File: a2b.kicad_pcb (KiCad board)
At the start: 2 copper layers, 58.4 x 67.9 mm, 16 parts, among them J1 M20-9990246

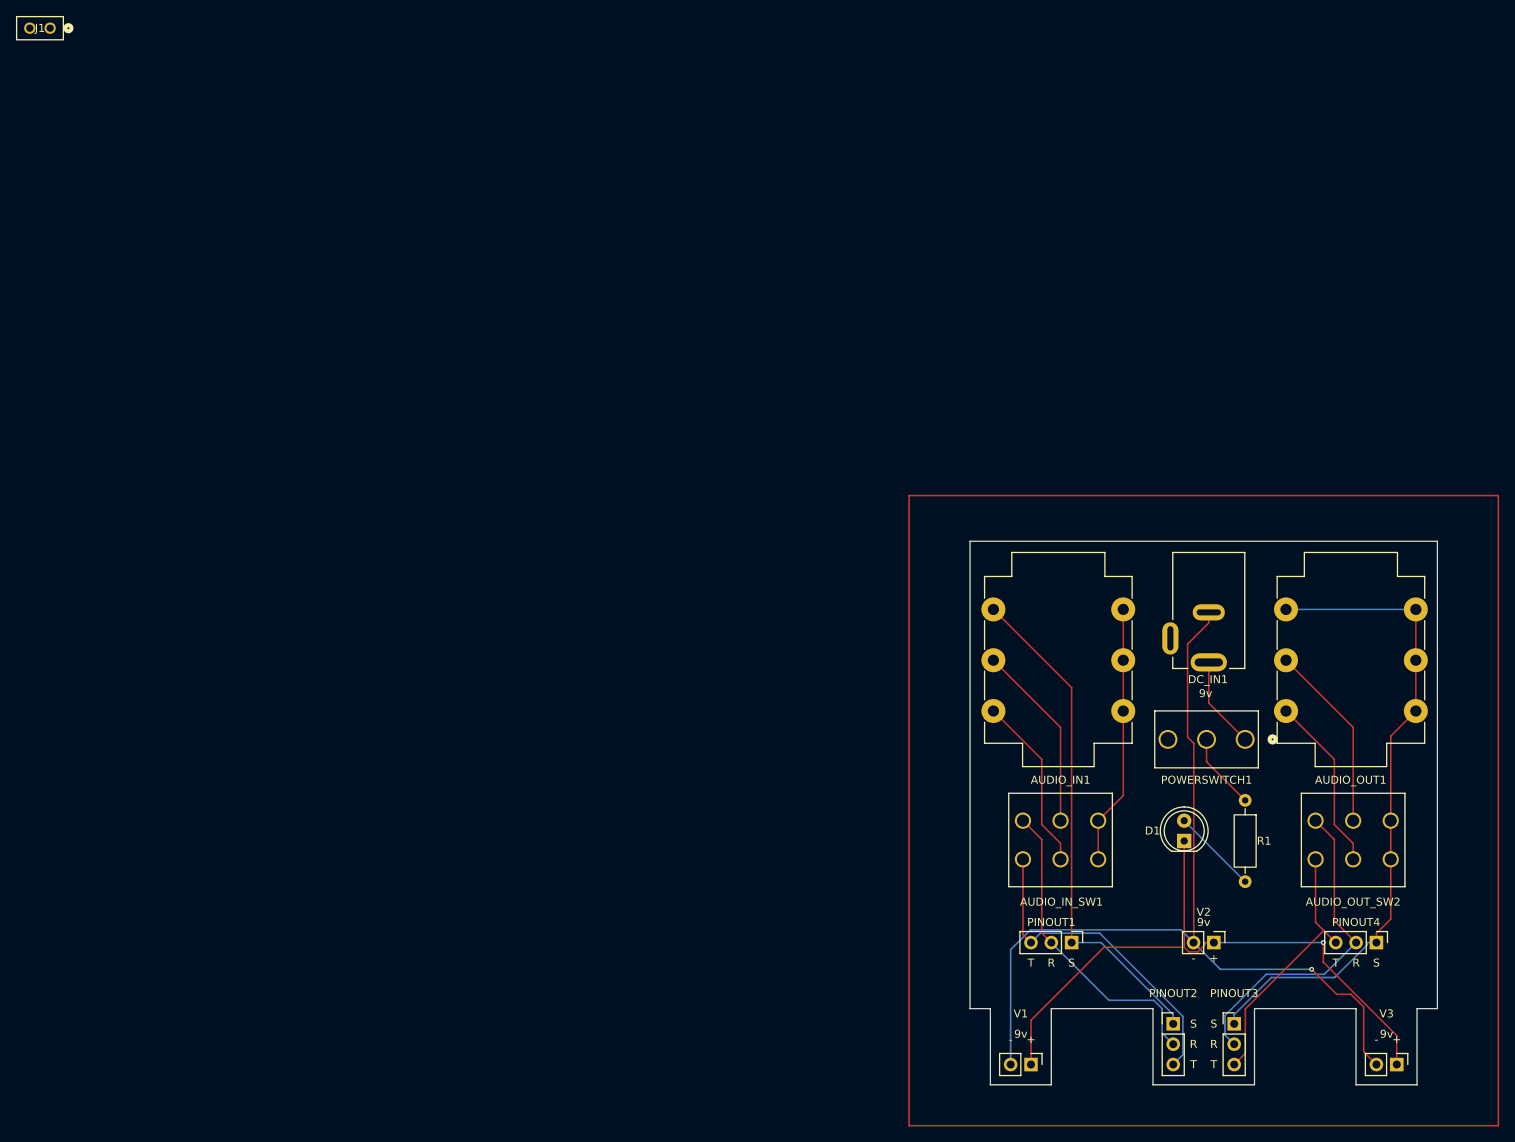
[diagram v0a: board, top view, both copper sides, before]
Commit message: swap to dip switches Signed-off-by: MrMentalFlower <samuelejpike@gmail.com>
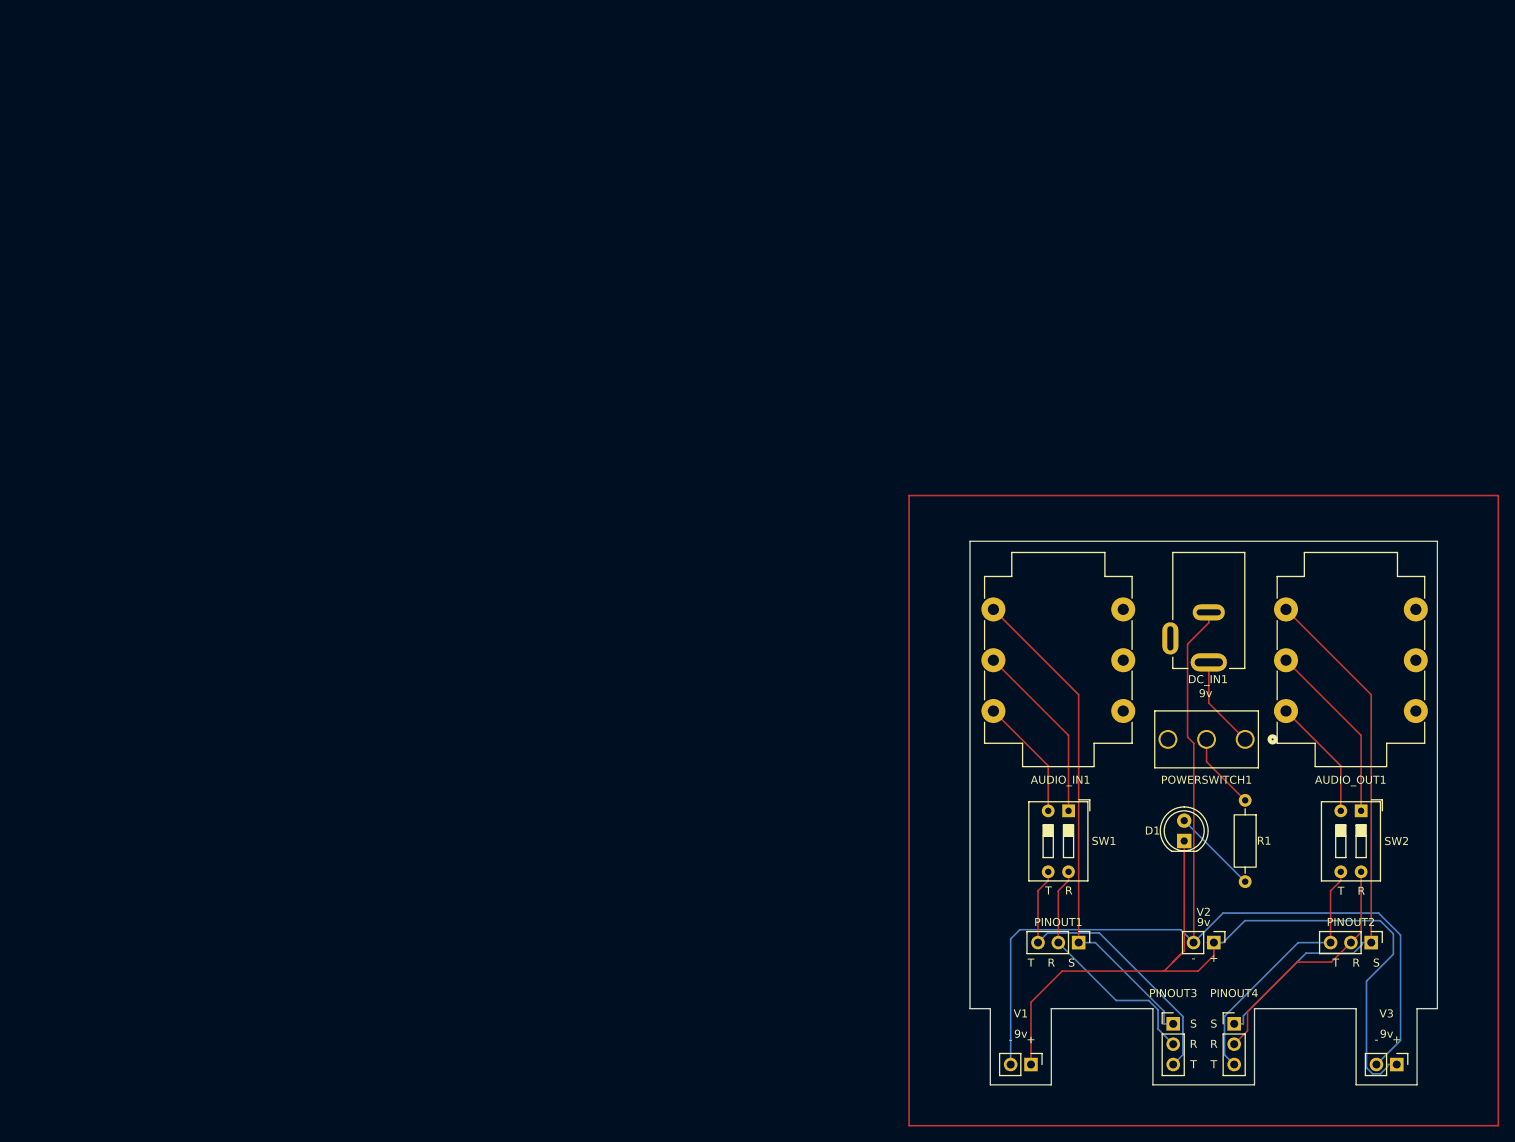
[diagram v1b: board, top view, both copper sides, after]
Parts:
- removed AUDIO_IN_SW1, AUDIO_OUT_SW2: ANT21SECQE, ANT21SECQE:SW6_ANT21SECQE_CRS
- removed J1: M20-9990246, M20-9990246:CONN2_M20-999_1x2_HRW
- added SW1: SW_DIP_x02, Button_Switch_THT:SW_DIP_SPSTx02_Slide_9.78x7.26mm_W7.62mm_P2.54mm, F.Cu at (131.7, 100.4)
- added SW2: SW_DIP_x02, Button_Switch_THT:SW_DIP_SPSTx02_Slide_9.78x7.26mm_W7.62mm_P2.54mm, F.Cu at (168.3, 100.4)
- moved PINOUT1 0.88 mm to (133.0, 116.8)
- moved PINOUT2 0.65 mm to (169.5, 116.8)
- renumbered PINOUT4 to PINOUT2, PINOUT2 to PINOUT3, PINOUT3 to PINOUT4
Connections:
- AUDIO_IN1 pad RN: Net-(AUDIO_IN1-PadRN) -> unconnected-(AUDIO_IN1-PadRN)
- AUDIO_IN1 pad SN: Net-(AUDIO_IN1-PadRN) -> unconnected-(AUDIO_IN1-PadSN)
- AUDIO_IN1 pad TN: Net-(AUDIO_IN1-PadRN) -> unconnected-(AUDIO_IN1-PadTN)
- AUDIO_OUT1 pad RN: Net-(AUDIO_OUT1-PadRN) -> unconnected-(AUDIO_OUT1-PadRN)
- AUDIO_OUT1 pad S: Net-(AUDIO_OUT1-PadRN) -> Net-(AUDIO_OUT1-PadS)
- AUDIO_OUT1 pad SN: Net-(AUDIO_OUT1-PadRN) -> unconnected-(AUDIO_OUT1-PadSN)
- AUDIO_OUT1 pad TN: Net-(AUDIO_OUT1-PadRN) -> unconnected-(AUDIO_OUT1-PadTN)
- PINOUT2 pad 1: Net-(AUDIO_OUT1-PadRN) -> Net-(AUDIO_OUT1-PadS)
- PINOUT4 pad 1: Net-(AUDIO_OUT1-PadRN) -> Net-(AUDIO_OUT1-PadS)
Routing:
- net Net-(AUDIO_OUT1-PadRN): track 82.7 -> 0.00 mm
- net Net-(AUDIO_OUT1-PadS): track 0.00 -> 68.1 mm
- net Net-(AUDIO_IN1-PadRN): track 32.5 -> 0.00 mm
- net Net-(D1-K): track 79.1 -> 103.9 mm, vias 1 -> 0
- net Net-(DC_IN1-PadSLEEVE): track 114.1 -> 128.4 mm, vias 1 -> 0
- net Net-(PINOUT2-Pad2): track 41.6 -> 30.6 mm
- net Net-(PINOUT1-Pad2): track 39.0 -> 30.4 mm
- net Net-(AUDIO_OUT1-PadT): track 22.0 -> 15.3 mm
- net Net-(AUDIO_IN1-PadT): track 22.0 -> 15.3 mm
- net Net-(PINOUT1-Pad3): track 41.1 -> 38.8 mm
- net Net-(AUDIO_OUT1-PadR): track 23.5 -> 22.7 mm
- net Net-(AUDIO_IN1-PadR): track 23.5 -> 22.7 mm

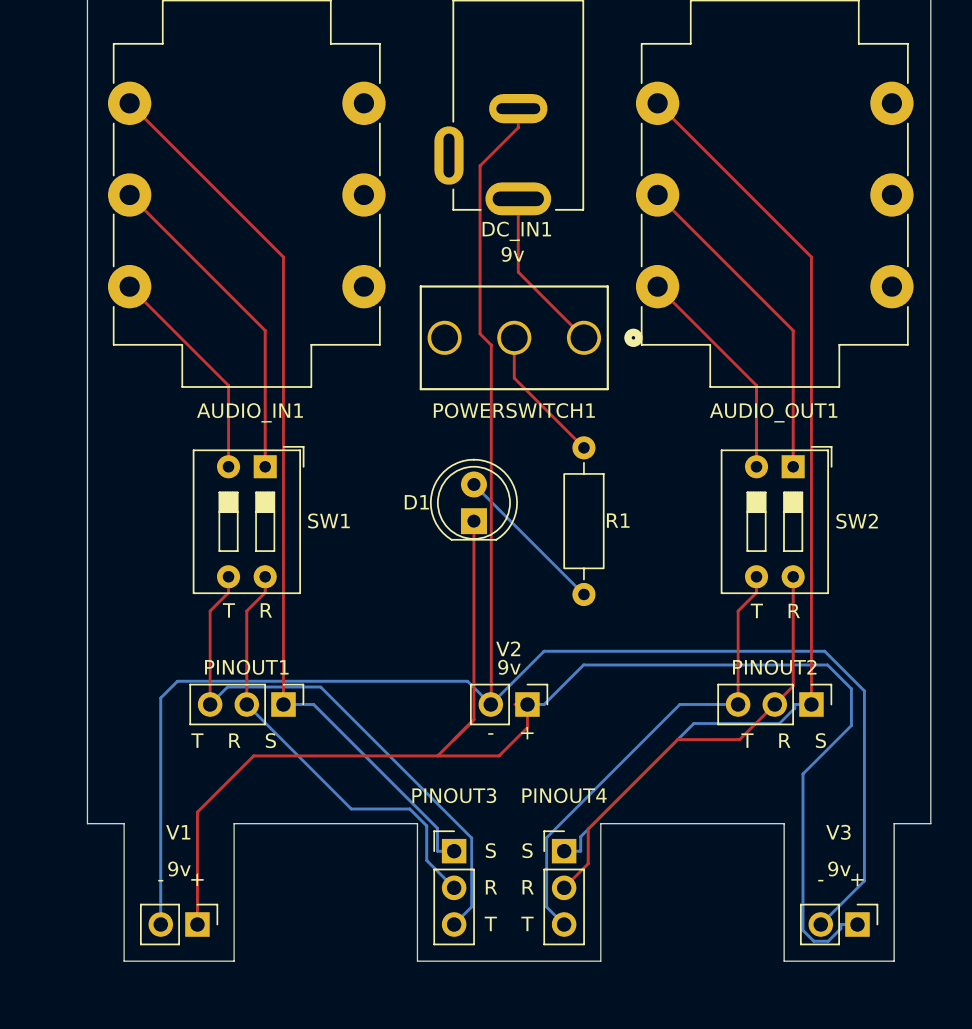
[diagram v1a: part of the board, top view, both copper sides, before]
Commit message: update dips switches and silk screen
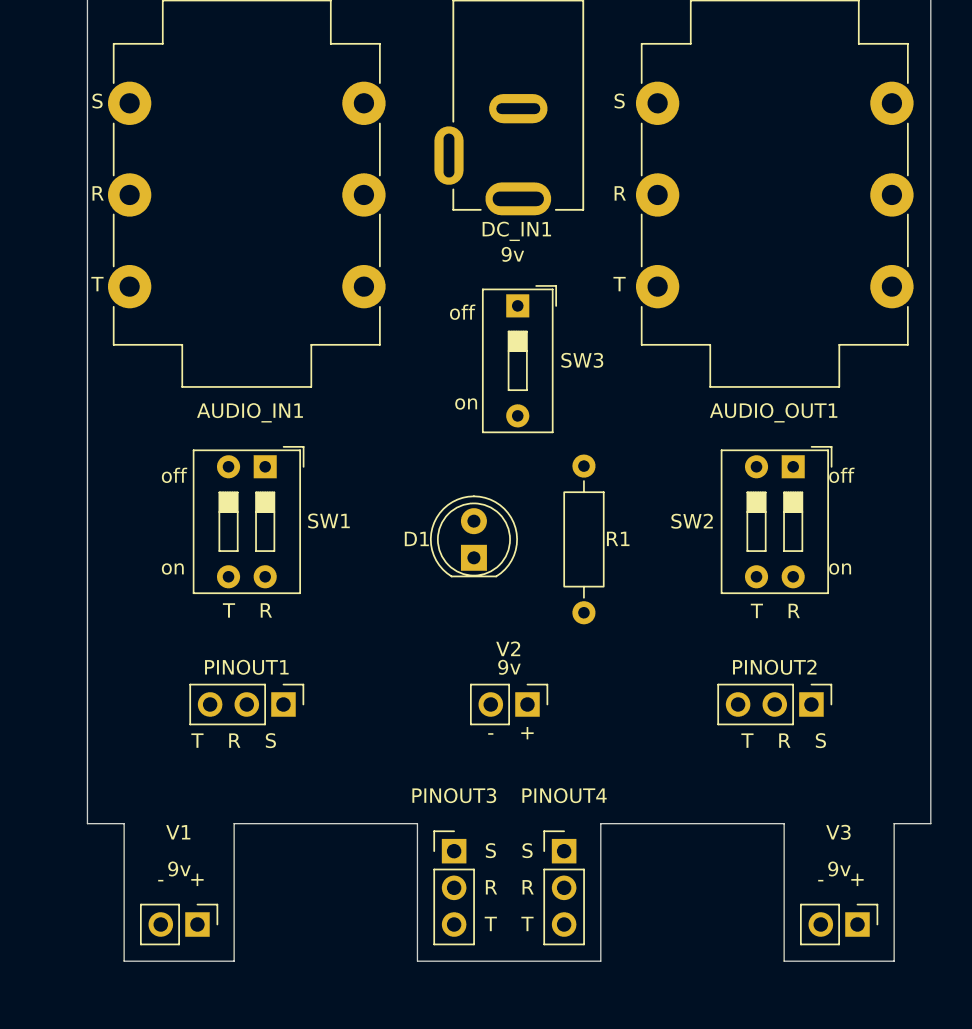
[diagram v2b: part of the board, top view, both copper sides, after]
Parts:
- removed POWERSWITCH1: ANT13SECQE, footprints:ANT13SEC_CRS
- added SW3: SW_DIP_x01, Button_Switch_THT:SW_DIP_SPSTx01_Slide_9.78x4.72mm_W7.62mm_P2.54mm, F.Cu at (149.2, 89.2)
- moved D1 2.54 mm to (146.2, 106.7)
- moved R1 1.27 mm to (153.8, 100.3)
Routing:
- net Net-(DC_IN1-PadSLEEVE): track 128.4 -> 0.00 mm
- net Net-(D1-K): track 103.9 -> 0.00 mm
- net Net-(AUDIO_OUT1-PadS): track 68.1 -> 0.00 mm
- net Net-(AUDIO_IN1-PadS): track 63.0 -> 0.00 mm
- net Net-(PINOUT1-Pad3): track 38.8 -> 0.00 mm
- net /Net-(PINOUT2-Pad3): track 33.0 -> 0.00 mm
- net /Net-(PINOUT2-Pad2): track 30.6 -> 0.00 mm
- net Net-(PINOUT1-Pad2): track 30.4 -> 0.00 mm
- net Net-(AUDIO_IN1-PadR): track 22.7 -> 0.00 mm
- net Net-(AUDIO_OUT1-PadR): track 22.7 -> 0.00 mm
- net Net-(AUDIO_IN1-PadT): track 15.3 -> 0.00 mm
- net Net-(AUDIO_OUT1-PadT): track 15.3 -> 0.00 mm
- net Net-(DC_IN1-PadPIN): track 11.5 -> 0.00 mm
- net Net-(D1-A): track 10.8 -> 0.00 mm
- net Net-(R1-Pad1): track 9.62 -> 0.00 mm
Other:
- board text added: "off"
- board text added: "on"

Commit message: updates
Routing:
- net Net-(DC_IN1-PadSLEEVE): track 0.00 -> 112.8 mm
- net Net-(D1-K): track 0.00 -> 83.4 mm
- net Net-(AUDIO_OUT1-PadS): track 0.00 -> 68.2 mm, vias 0 -> 1
- net Net-(AUDIO_IN1-PadS): track 0.00 -> 62.8 mm
- net Net-(PINOUT1-Pad3): track 0.00 -> 35.5 mm
- net /Net-(PINOUT2-Pad3): track 0.00 -> 33.0 mm
- net Net-(PINOUT1-Pad2): track 0.00 -> 30.7 mm
- net /Net-(PINOUT2-Pad2): track 0.00 -> 30.6 mm
- net Net-(AUDIO_IN1-PadR): track 0.00 -> 22.7 mm
- net Net-(AUDIO_OUT1-PadR): track 0.00 -> 22.7 mm
- net Net-(AUDIO_IN1-PadT): track 0.00 -> 15.3 mm
- net Net-(AUDIO_OUT1-PadT): track 0.00 -> 15.3 mm
- net Net-(D1-A): track 0.00 -> 10.2 mm
- net Net-(DC_IN1-PadPIN): track 0.00 -> 7.43 mm
- net Net-(R1-Pad1): track 0.00 -> 6.03 mm

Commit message: swap switch
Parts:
- SW3: value SW_DIP_x01 -> SW_DIP_x02; footprint Button_Switch_THT:SW_DIP_SPSTx01_Slide_9.78x4.72mm_W7.62mm_P2.54mm -> Button_Switch_THT:SW_DIP_SPSTx02_Slide_9.78x7.26mm_W7.62mm_P2.54mm
- moved SW3 1.37 mm to (150.6, 89.2)
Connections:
- SW3 pad 2: Net-(R1-Pad1) -> Net-(DC_IN1-PadSLEEVE)
- V1 pad 2: Net-(DC_IN1-PadSLEEVE) -> Net-(SW3-Pad3)
- V2 pad 2: Net-(DC_IN1-PadSLEEVE) -> Net-(SW3-Pad3)
- V3 pad 2: Net-(DC_IN1-PadSLEEVE) -> Net-(SW3-Pad3)
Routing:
- net Net-(DC_IN1-PadSLEEVE): track 112.8 -> 15.3 mm
- net Net-(SW3-Pad3): track 0.00 -> 90.4 mm
- net Net-(R1-Pad1): track 6.03 -> 5.31 mm
- net Net-(DC_IN1-PadPIN): track 7.43 -> 7.93 mm
